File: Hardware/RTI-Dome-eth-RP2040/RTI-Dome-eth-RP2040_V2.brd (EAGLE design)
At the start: 111.1 x 76.3 mm, 104 parts, among them IC2 24LC128T-I_SN, IC3 FT232RL, IC4 RASPBERRY_PI_PICO, IC8 REG1117-3.3V, IC9 REG1117-5V, J2 XT60PW-M, U1 W5500, X13 PN61729-S, X9 J1011F21PNL

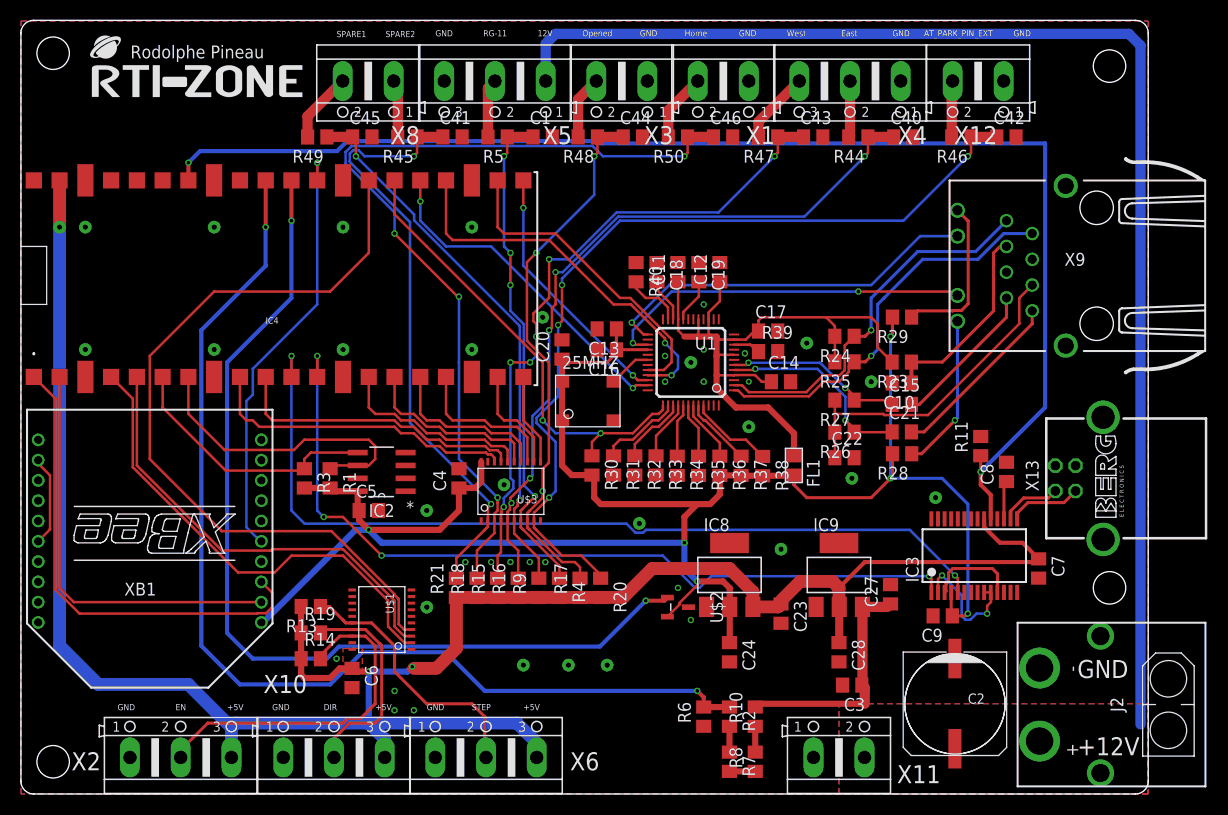
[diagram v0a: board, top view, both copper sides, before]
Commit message: Added transistor for stepper controller output
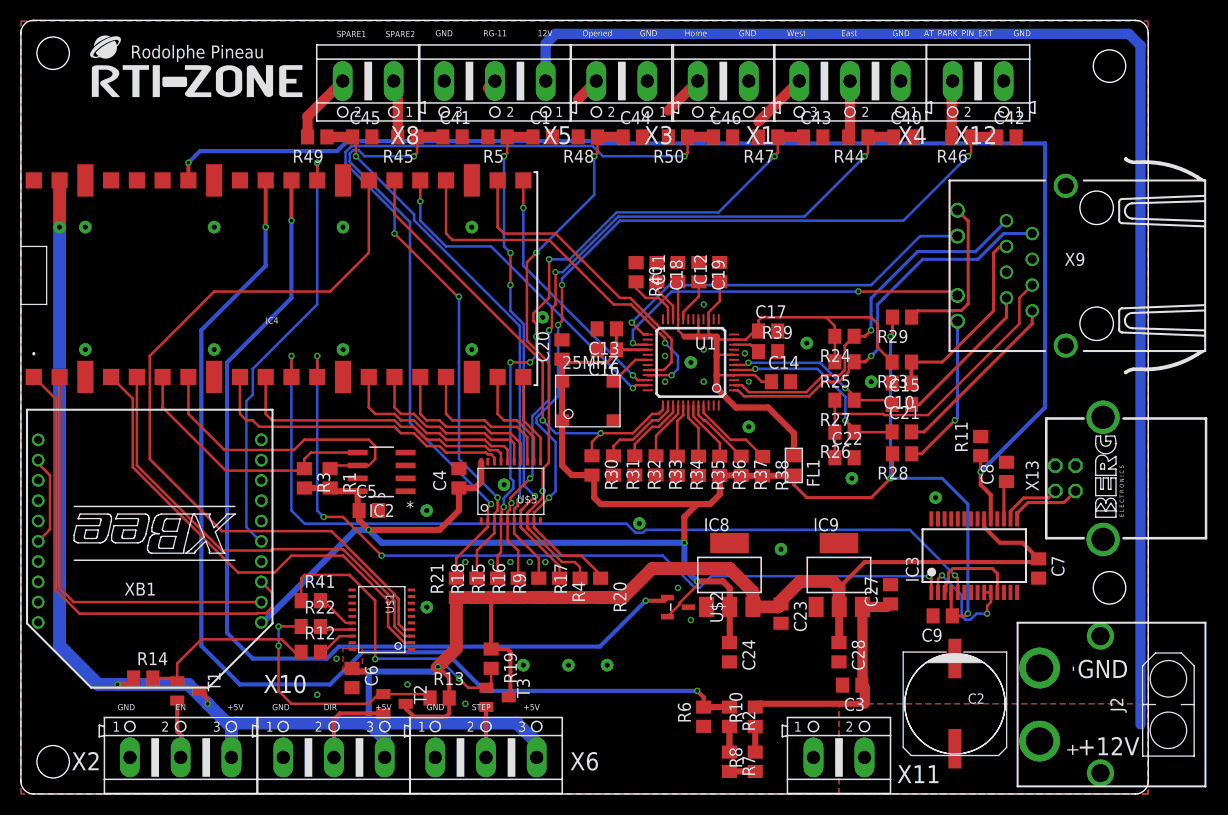
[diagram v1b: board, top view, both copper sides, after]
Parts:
- added R12, R22, R41: 1K, rcl:R0805
- added T1, T2, T3: (no value), transistor:SOT23-BEC
- IC2: value 24LC128T-I_SN -> 24LC64T-I/SN; device rti:SOIC127P600X175-8N -> Microchip_By_element14_Batch_1:SOIC127P600X175-8N
- R13, R14, R19: value 1K -> 10K
- moved R19 18.0 mm to (46.4, 13.3), turned to 270 degrees
- moved R14 16.6 mm to (12.1, 11.4)
- moved R13 15.6 mm to (41.3, 9.46), turned to 0 degrees
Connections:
- removed net AT_PARK_PIN_LOOP: U$1.P$5
- removed net AT_PARK_PIN_LOOP_EXT: U$1.P$15
- new net DIR-5V_PULLUP: R13.1, R22.1, T2.B
- new net DIR_5V_OUT: T2.E, X10.2
- new net EN-5V_PULLUP: R12.1, R14.2, T1.B
- new net EN_5V_OUT: T1.E, X2.2
- new net STEP-5V_PULLUP: R19.2, R41.1, T3.B
- new net STEP_5V_OUT: T3.E, X6.2
- net BUTTON_EAST_OPEN-IN_EXT: no longer R44.2
- net BUTTON_WEST_CLOSE-IN_EXT: no longer R47.2
- net GND: now also U$1.P$5
- net HOME_SHUTTER_CLOSED-IN_EXT: no longer R50.2
- net M_DIR_5V: now also R22.2; no longer R19.2, X10.2
- net M_EN_5V: now also R12.2; no longer R14.2, X2.2
- net M_STEP_5V: now also R41.2; no longer R13.1, X6.2
- net RG-11-IN_EXT: no longer R5.2
- net SHUTTER_OPENED-IN_EXT: no longer R48.2
- net VCC: now also T1.C, T2.C
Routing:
- net STEP-5V_PULLUP: track 0.00 -> 30.7 mm, vias 0 -> 2
- net M_EN_5V: track 34.4 -> 3.78 mm
- net DIR-5V_PULLUP: track 0.00 -> 24.6 mm, vias 0 -> 2
- net M_STEP_5V: track 27.2 -> 4.03 mm
- net M_DIR_5V: track 21.8 -> 3.25 mm
- net EN-5V_PULLUP: track 0.00 -> 18.0 mm
- net VCC: track 216.1 -> 229.4 mm, vias 3 -> 5
- net DIR_5V_OUT: track 0.00 -> 8.87 mm
- net EN_5V_OUT: track 0.00 -> 5.86 mm
- net STEP_5V_OUT: track 0.00 -> 4.99 mm
- net RG-11-IN_EXT: track 5.80 -> 0.98 mm
- net SHUTTER_OPENED-IN_EXT: track 6.25 -> 2.54 mm
- net HOME_SHUTTER_CLOSED-IN_EXT: track 6.71 -> 4.11 mm
- net BUTTON_WEST_CLOSE-IN_EXT: track 7.17 -> 5.68 mm

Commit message: Fix some issue after the schematics snap to grid.
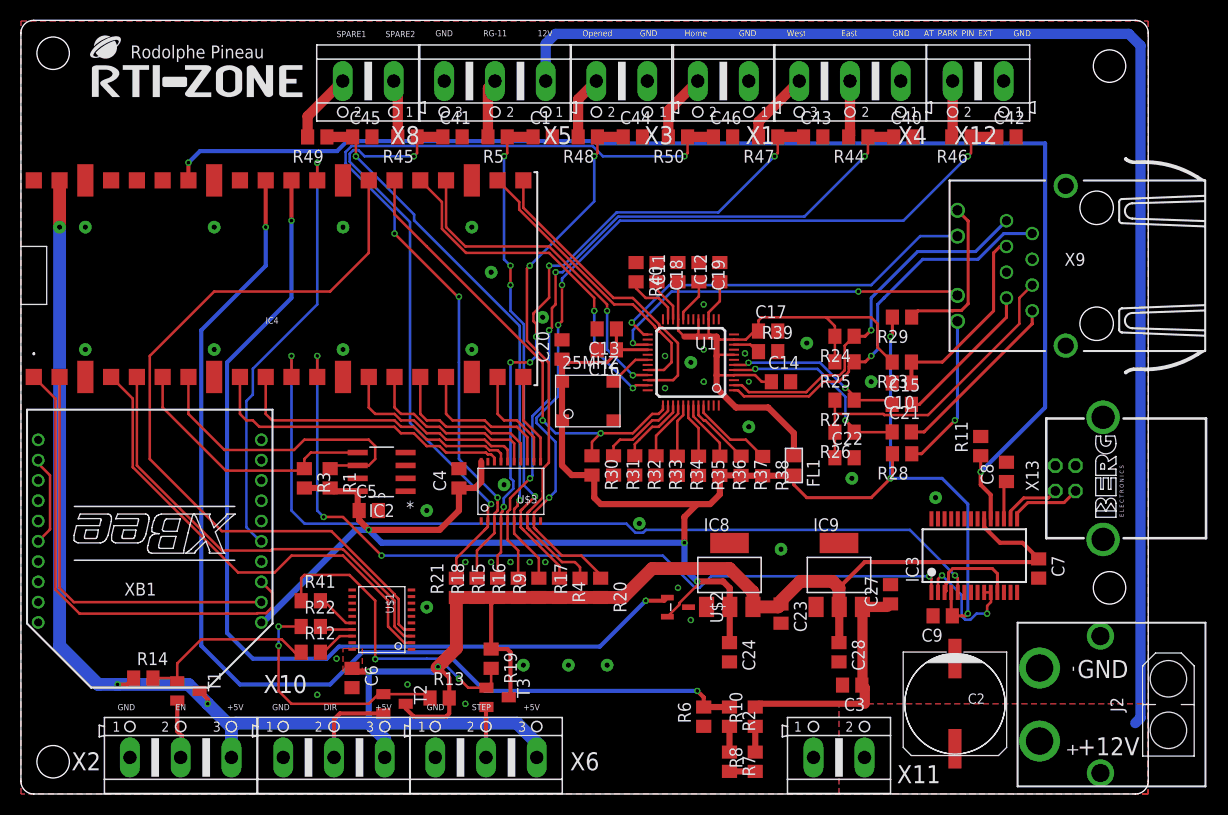
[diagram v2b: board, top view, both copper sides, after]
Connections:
- net BUTTON_EAST_OPEN-IN_EXT: now also R44.2
- net BUTTON_WEST_CLOSE-IN_EXT: now also R47.2
- net HOME_SHUTTER_CLOSED-IN_EXT: now also R50.2
- net RG-11-IN_EXT: now also R5.2
- net SHUTTER_OPENED-IN_EXT: now also R48.2
- net VCC: now also T3.C
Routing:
- net RG-11-IN_EXT: track 0.98 -> 5.80 mm
- net SCLK: track 37.9 -> 33.2 mm
- net SDI: track 25.4 -> 29.9 mm, vias 2 -> 0
- net SHUTTER_OPENED-IN_EXT: track 2.54 -> 6.25 mm
- net HOME_SHUTTER_CLOSED-IN_EXT: track 4.11 -> 6.71 mm
- net ETH_CS: track 31.3 -> 28.8 mm
- net SDO: track 33.4 -> 35.6 mm
- net BUTTON_WEST_CLOSE-IN_EXT: track 5.68 -> 7.17 mm
- net BUTTON_EAST_OPEN_5V: track 72.5 -> 72.4 mm, vias 5 -> 4
- net SHUTTER_OPENED_IN_5V: vias 3 -> 2

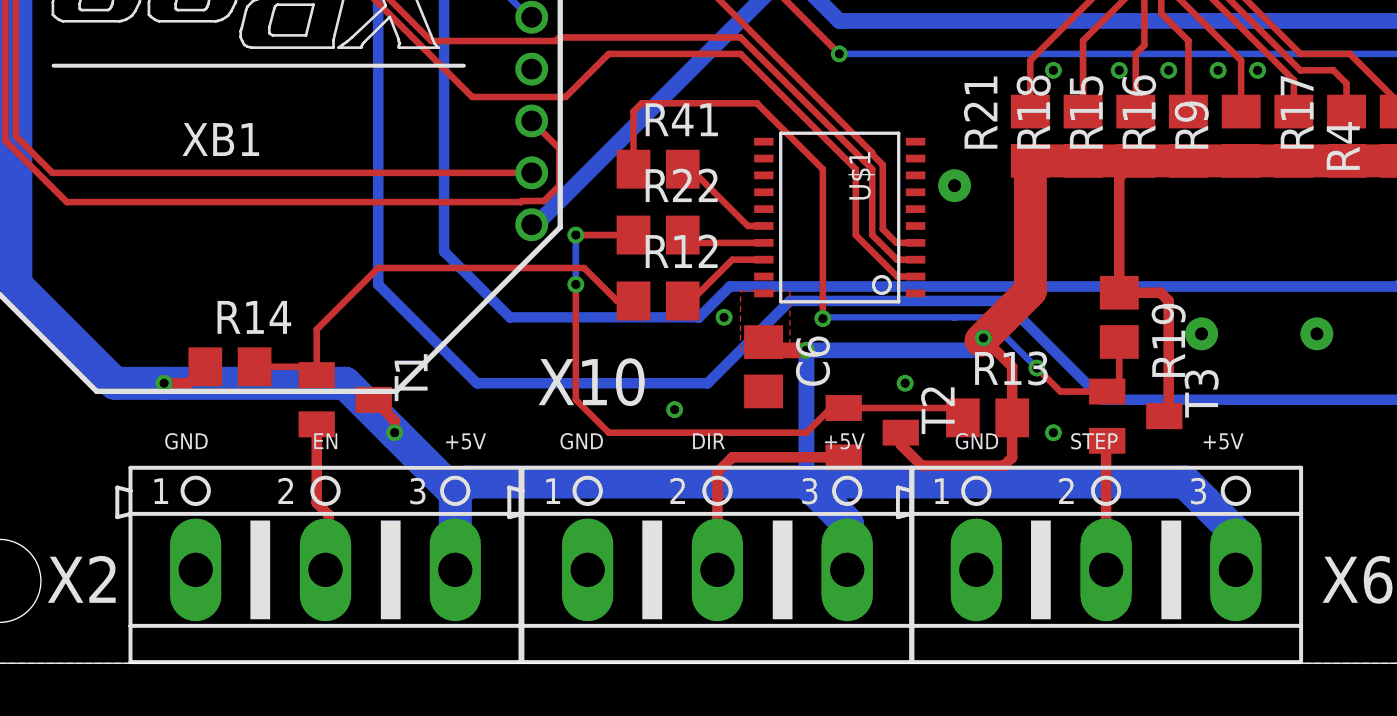
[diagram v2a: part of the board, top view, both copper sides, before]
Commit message: Remove unused pull-up
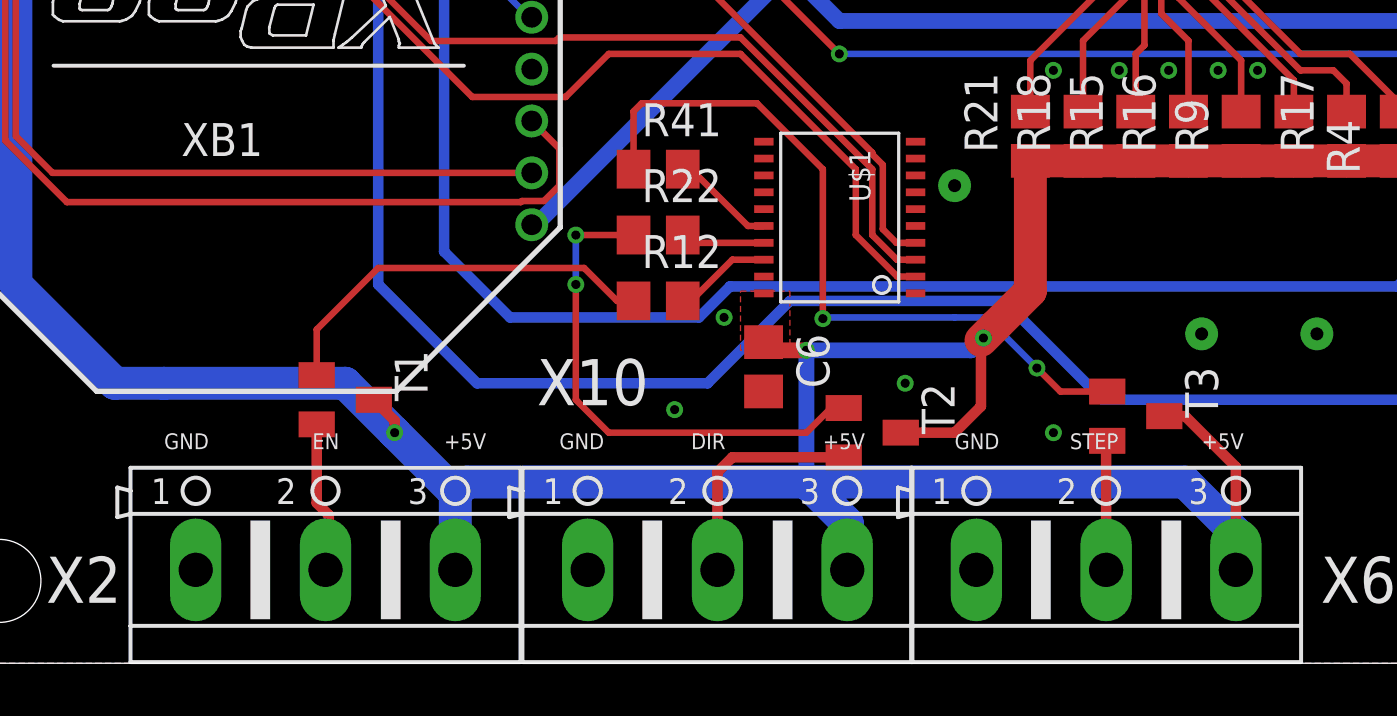
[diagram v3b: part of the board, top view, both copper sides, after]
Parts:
- removed R13, R14, R19: 10K, rcl:R0805
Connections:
- removed net DIR-5V_PULLUP: R13.1, R22.1, T2.B
- removed net EN-5V_PULLUP: R12.1, R14.2, T1.B
- removed net STEP-5V_PULLUP: R19.2, R41.1, T3.B
- new net DIR-5V_TR: R22.1, T2.B
- new net EN-5V_TR: R12.1, T1.B
- new net STEP-5V_TR: R41.1, T3.B
- net VCC: no longer R13.2, R14.1, R19.1
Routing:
- net STEP-5V_PULLUP: track 30.7 -> 0.00 mm, vias 2 -> 0
- net STEP-5V_TR: track 0.00 -> 28.6 mm, vias 0 -> 2
- net DIR-5V_PULLUP: track 24.6 -> 0.00 mm, vias 2 -> 0
- net DIR-5V_TR: track 0.00 -> 19.8 mm, vias 0 -> 2
- net EN-5V_PULLUP: track 18.0 -> 0.00 mm
- net EN-5V_TR: track 0.00 -> 15.5 mm
- net VCC: track 229.7 -> 219.2 mm, vias 5 -> 4
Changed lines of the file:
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@@
 <attribute name="VALUE" x="85.725" y="13.97" size="1.016" layer="27" rot="R270"/>
-</element>
-<element name="R13" library="rcl" library_urn="urn:adsk.eagle:library:334" package="R0805" package3d_urn="urn:adsk.eagle:package:23553/2" value="10K" x="41.275" y="9.4615" smashed="yes">
-<attribute name="MPN" value="RT0805FRE074K7L" x="41.275" y="9.4615" size="1.778" layer="27" display="off"/>
-<attribute name="NAME" x="40.64" y="10.7315" size="1.27" layer="25"/>
-<attribute name="POPULARITY" value="86" x="41.275" y="9.4615" size="1.778" layer="27" display="off"/>
-<attribute name="SPICEPREFIX" value="R" x="41.275" y="9.4615" size="1.778" layer="27" display="off"/>
-<attribute name="VALUE" x="40.64" y="6.9215" size="1.27" layer="27"/>
-</element>
-<element name="R14" library="rcl" library_urn="urn:adsk.eagle:library:334" package="R0805" package3d_urn="urn:adsk.eagle:package:23553/2" value="10K" x="12.065" y="11.43" smashed="yes">
-<attribute name="MPN" value="RT0805FRE074K7L" x="12.065" y="11.43" size="1.778" layer="27" display="off"/>
-<attribute name="NAME" x="11.43" y="12.7" size="1.27" layer="25"/>
-<attribute name="POPULARITY" value="86" x="12.065" y="11.43" size="1.778" layer="27" display="off"/>
-<attribute name="SPICEPREFIX" value="R" x="12.065" y="11.43" size="1.778" layer="27" display="off"/>
-<attribute name="VALUE" x="10.16" y="11.43" size="1.27" layer="27" rot="R180"/>
 </element>
 <element name="R15" library="rcl" library_urn="urn:adsk.eagle:library:334" package="R0805" package3d_urn="urn:adsk.eagle:package:23553/2" value="4.7K" x="46.99" y="20.32" smashed="yes" rot="R90">
@@
 <attribute name="SPICEPREFIX" value="R" x="44.958" y="20.32" size="1.778" layer="27" rot="R90" display="off"/>
 <attribute name="VALUE" x="47.498" y="19.685" size="1.27" layer="27" rot="R90"/>
-</element>
-<element name="R19" library="rcl" library_urn="urn:adsk.eagle:library:334" package="R0805" package3d_urn="urn:adsk.eagle:package:23553/2" value="10K" x="46.355" y="13.335" smashed="yes" rot="R270">
-<attribute name="MPN" value="RT0805FRE074K7L" x="46.355" y="13.335" size="1.778" layer="27" rot="R270" display="off"/>
-<attribute name="NAME" x="47.625" y="13.97" size="1.27" layer="25" rot="R270"/>
-<attribute name="POPULARITY" value="86" x="46.355" y="13.335" size="1.778" layer="27" rot="R270" display="off"/>
-<attribute name="SPICEPREFIX" value="R" x="46.355" y="13.335" size="1.778" layer="27" rot="R270" display="off"/>
-<attribute name="VALUE" x="46.45025" y="15.14475" size="1.27" layer="27" rot="R90"/>
 </element>
 <element name="R6" library="rcl" library_urn="urn:adsk.eagle:library:334" package="R0805" package3d_urn="urn:adsk.eagle:package:23553/2" value="100K 0.1%" x="67.31" y="7.62" smashed="yes" rot="R90">
@@
 <contactref element="T1" pad="C"/>
 <contactref element="T2" pad="C"/>
-<contactref element="R14" pad="1"/>
-<contactref element="R19" pad="1"/>
-<contactref element="R13" pad="2"/>
-<wire x1="46.355" y1="14.285" x2="46.355" y2="18.735" width="0.4064" layer="1"/>
-<wire x1="46.355" y1="18.735" x2="46.99" y2="19.37" width="0.4064" layer="1"/>
-<wire x1="46.355" y1="14.285" x2="47.945" y2="14.285" width="0.4064" layer="1"/>
-<wire x1="47.945" y1="14.285" x2="48.26" y2="13.97" width="0.4064" layer="1"/>
-<wire x1="41.115" y1="12.54" x2="42.225" y2="11.43" width="0.4064" layer="1"/>
-<wire x1="42.225" y1="11.43" x2="42.225" y2="9.4615" width="0.4064" layer="1"/>
-<wire x1="42.225" y1="9.4615" x2="42.225" y2="7.935" width="0.4064" layer="1"/>
-<wire x1="42.225" y1="7.935" x2="41.91" y2="7.62" width="0.4064" layer="1"/>
-<wire x1="41.91" y1="7.62" x2="38.735" y2="7.62" width="0.4064" layer="1"/>
-<wire x1="38.735" y1="7.62" x2="37.93" y2="8.425" width="0.4064" layer="1"/>
-<wire x1="37.93" y1="8.425" x2="37.93" y2="8.89" width="0.4064" layer="1"/>
-<wire x1="11.115" y1="11.43" x2="10.48" y2="10.795" width="0.4064" layer="1"/>
-<wire x1="10.48" y1="10.795" x2="9.525" y2="10.795" width="0.4064" layer="1"/>
-<via x="9.525" y="10.795" extent="1-16" drill="0.35"/>
 <wire x1="17.61" y1="10.16" x2="18.415" y2="9.355" width="0.4064" layer="1"/>
 <wire x1="18.415" y1="9.355" x2="18.415" y2="8.89" width="0.4064" layer="1"/>
 <via x="18.415" y="8.89" extent="1-16" drill="0.35"/>
 <contactref element="T3" pad="C"/>
-<wire x1="48.26" y1="13.97" x2="48.26" y2="9.695" width="0.4064" layer="1"/>
-<wire x1="48.26" y1="9.695" x2="48.09" y2="9.525" width="0.4064" layer="1"/>
+<wire x1="37.93" y1="8.89" x2="40.005" y2="8.89" width="0.4064" layer="1"/>
+<wire x1="40.005" y1="8.89" x2="41.021" y2="9.906" width="0.4064" layer="1"/>
+<wire x1="41.021" y1="9.906" x2="41.021" y2="12.446" width="0.4064" layer="1"/>
+<wire x1="48.09" y1="9.525" x2="48.895" y2="9.525" width="0.4064" layer="1"/>
+<wire x1="50.8508" y1="7.5692" x2="50.8508" y2="3.6" width="0.4064" layer="1"/>
+<wire x1="48.895" y1="9.525" x2="50.8508" y2="7.5692" width="0.4064" layer="1"/>
 </signal>
 <signal name="N$2">
@@
 <wire x1="98.205" y1="27.12" x2="98.205" y2="27.67" width="0.3048" layer="1"/>
 </signal>
-<signal name="DIR-5V_PULLUP">
+<signal name="DIR-5V_TR">
 <contactref element="R22" pad="1"/>
 <contactref element="T2" pad="B"/>
-<contactref element="R13" pad="1"/>
 <wire x1="27.625" y1="16.51" x2="25.4" y2="16.51" width="0.254" layer="1"/>
 <via x="25.4" y="16.51" extent="1-16" drill="0.35"/>
@@
 <wire x1="35.24" y1="9.84" x2="35.73" y2="9.84" width="0.4064" layer="1"/>
 <wire x1="34.29" y1="8.89" x2="35.24" y2="9.84" width="0.254" layer="1"/>
-<wire x1="35.73" y1="9.84" x2="39.9465" y2="9.84" width="0.254" layer="1"/>
-<wire x1="39.9465" y1="9.84" x2="40.325" y2="9.4615" width="0.254" layer="1"/>
-</signal>
-<signal name="STEP-5V_PULLUP">
+</signal>
+<signal name="STEP-5V_TR">
 <contactref element="R41" pad="1"/>
 <contactref element="T3" pad="B"/>
-<contactref element="R19" pad="2"/>
 <wire x1="27.625" y1="19.05" x2="27.625" y2="21.275" width="0.254" layer="1"/>
 <wire x1="27.625" y1="21.275" x2="27.94" y2="21.59" width="0.254" layer="1"/>
@@
 <via x="43.18" y="11.382" extent="1-16" drill="0.35"/>
 <wire x1="34.925" y1="19.05" x2="34.925" y2="13.287" width="0.254" layer="1"/>
-<wire x1="46.355" y1="12.385" x2="46.355" y2="10.94" width="0.254" layer="1"/>
-<wire x1="46.355" y1="10.94" x2="45.89" y2="10.475" width="0.254" layer="1"/>
 <wire x1="44.087" y1="10.475" x2="43.18" y2="11.382" width="0.254" layer="1"/>
 <wire x1="45.89" y1="10.475" x2="44.087" y2="10.475" width="0.254" layer="1"/>
 <wire x1="41.227" y1="13.335" x2="43.18" y2="11.382" width="0.254" layer="16"/>
 </signal>
-<signal name="EN-5V_PULLUP">
+<signal name="EN-5V_TR">
 <contactref element="R12" pad="1"/>
 <contactref element="T1" pad="B"/>
-<contactref element="R14" pad="2"/>
 <wire x1="15.41" y1="12.87" x2="15.41" y2="11.11" width="0.254" layer="1"/>
 <wire x1="27.625" y1="13.97" x2="26.99" y2="13.97" width="0.254" layer="1"/>
@@
 <wire x1="25.72" y1="15.24" x2="17.78" y2="15.24" width="0.254" layer="1"/>
 <wire x1="17.78" y1="15.24" x2="15.41" y2="12.87" width="0.254" layer="1"/>
-<wire x1="13.015" y1="11.43" x2="15.09" y2="11.43" width="0.254" layer="1"/>
-<wire x1="15.09" y1="11.43" x2="15.41" y2="11.11" width="0.254" layer="1"/>
 </signal>
 <signal name="EN_5V_OUT">
